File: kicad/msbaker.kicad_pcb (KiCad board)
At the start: 4 copper layers, 14 x 62 mm, 41 parts, among them J1 USB_B_Micro, J2 Micro_SD_Card, J3 GPIO, M2 MountingHole_2.2mm_M2_ISO1458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, U1 MIC5365-3.3YC5, U2 W25Q128JVS, U3 RP2040, U4 LSM6DSO32, Y1 12MHz

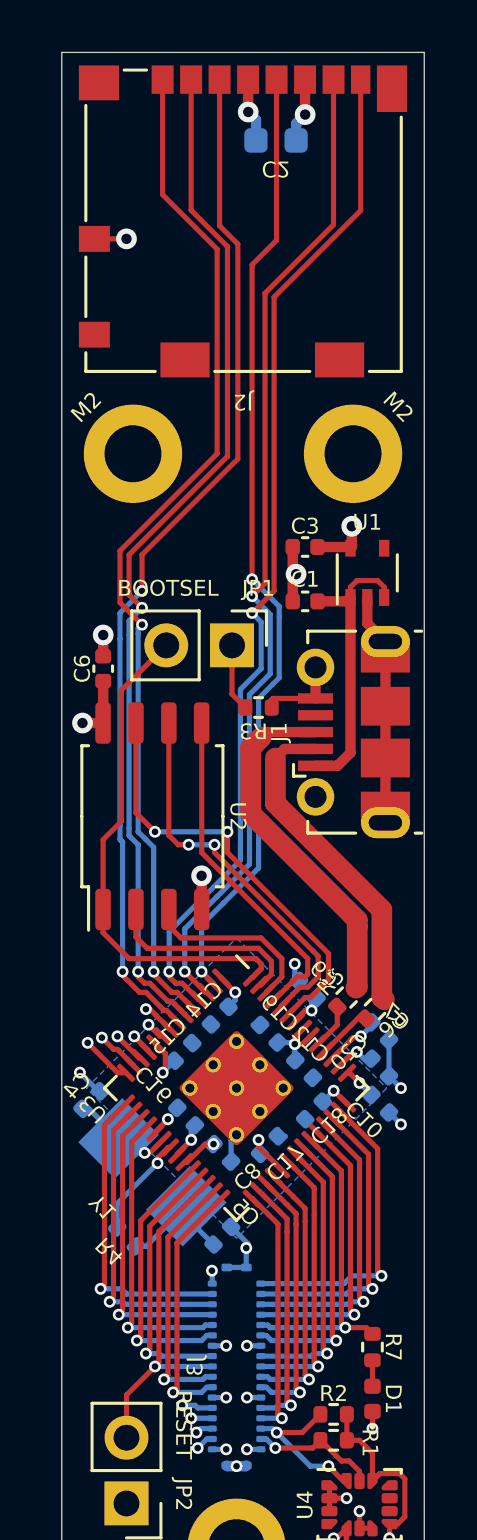
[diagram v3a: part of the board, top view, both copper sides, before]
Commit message: Fixed DRC violations
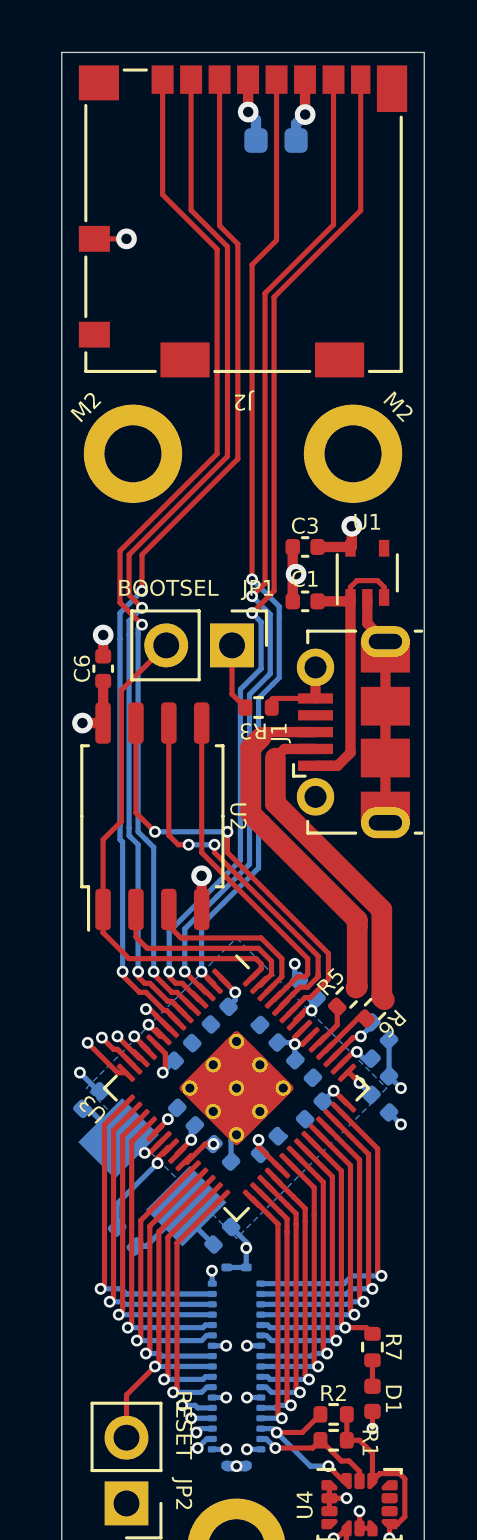
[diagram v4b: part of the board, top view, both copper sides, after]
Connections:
- J3 pad GND: (no net) -> GND
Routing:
- net GND: track 37.7 -> 38.5 mm, vias 21 -> 22
- net (no net): track 0.77 -> 0.00 mm, vias 1 -> 0
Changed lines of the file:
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@@
     (property "Sheetname" "")
     (attr smd)
-    (fp_text reference "C9" (at 0 0.848528 315 unlocked) (layer "F.SilkS")
+    (fp_text reference "C9" (at 0 0.848528 315 unlocked) (layer "B.SilkS")
       (effects (font (size 0.61 0.61) (thickness 0.0762)) (justify mirror))
     )
@@
     (property "Sheetname" "")
     (attr smd)
-    (fp_text reference "C19" (at 0.282843 0.848528 315 unlocked) (layer "F.SilkS")
+    (fp_text reference "C19" (at 0.282843 0.848528 315 unlocked) (layer "B.SilkS")
       (effects (font (size 0.61 0.61) (thickness 0.0762)) (justify mirror))
     )
@@
     (property "Sheetname" "")
     (attr smd)
-    (fp_text reference "C10" (at 0 0.848528 135 unlocked) (layer "F.SilkS")
+    (fp_text reference "C10" (at 0 0.848528 135 unlocked) (layer "B.SilkS")
       (effects (font (size 0.61 0.61) (thickness 0.0762)) (justify mirror))
     )
@@
     (property "Sheetname" "")
     (attr smd)
-    (fp_text reference "C12" (at -0.50995 -0.848528 -45 unlocked) (layer "F.SilkS")
+    (fp_text reference "C12" (at -0.50995 -0.848528 -45 unlocked) (layer "B.SilkS")
       (effects (font (size 0.61 0.61) (thickness 0.0762)) (justify mirror))
     )
@@
     (property "Sheetname" "")
     (attr smd)
-    (fp_text reference "C18" (at 0.02038 -0.813173 -135 unlocked) (layer "F.SilkS")
+    (fp_text reference "C18" (at 0.02038 -0.813173 -135 unlocked) (layer "B.SilkS")
       (effects (font (size 0.61 0.61) (thickness 0.0762)) (justify mirror))
     )
@@
     (property "Sheetname" "")
     (attr smd)
-    (fp_text reference "C15" (at 0 -0.848528 45 unlocked) (layer "F.SilkS")
+    (fp_text reference "C15" (at 0 -0.848528 45 unlocked) (layer "B.SilkS")
       (effects (font (size 0.61 0.61) (thickness 0.0762)) (justify mirror))
     )
@@
     (property "Sheetname" "")
     (attr smd)
-    (fp_text reference "C16" (at 1.767767 0 135 unlocked) (layer "F.SilkS")
+    (fp_text reference "C16" (at 1.767767 0 135 unlocked) (layer "B.SilkS")
       (effects (font (size 0.61 0.61) (thickness 0.0762)) (justify mirror))
     )
@@
     (property "Sheetname" "")
     (attr smd)
-    (fp_text reference "C17" (at -0.035355 0.883883 225 unlocked) (layer "F.SilkS")
+    (fp_text reference "C17" (at -0.035355 0.883883 225 unlocked) (layer "B.SilkS")
       (effects (font (size 0.61 0.61) (thickness 0.0762)) (justify mirror))
     )
@@
     (property "Sheetname" "")
     (attr smd)
-    (fp_text reference "J3" (at 0 1.6 90 unlocked) (layer "F.SilkS")
+    (fp_text reference "J3" (at 0 1.6 90 unlocked) (layer "B.SilkS")
       (effects (font (size 0.61 0.61) (thickness 0.0762)) (justify mirror))
     )
@@
     (pad "34" smd roundrect (at 3.2 0.9375 270) (size 0.24 0.35) (layers "B.Cu" "B.Paste" "B.Mask") (roundrect_rratio 0.25)
       (net 2 "GND") (pinfunction "Pin_34") (pintype "passive"))
-    (pad "GND" smd roundrect (at 3.825 0.375 270) (size 0.3 0.42) (layers "B.Cu" "B.Paste" "B.Mask") (roundrect_rratio 0.25))
-    (pad "GND" smd roundrect (at -3.825 0.375 270) (size 0.3 0.42) (layers "B.Cu" "B.Paste" "B.Mask") (roundrect_rratio 0.25))
-    (pad "GND" smd roundrect (at -3.825 -0.375 270) (size 0.3 0.42) (layers "B.Cu" "B.Paste" "B.Mask") (roundrect_rratio 0.25))
-    (pad "GND" smd roundrect (at 3.825 -0.375 270) (size 0.3 0.42) (layers "B.Cu" "B.Paste" "B.Mask") (roundrect_rratio 0.25))
+    (pad "GND" smd roundrect (at 3.825 0.375 270) (size 0.3 0.42) (layers "B.Cu" "B.Paste" "B.Mask") (roundrect_rratio 0.25)
+      (net 2 "GND"))
+    (pad "GND" smd roundrect (at -3.825 0.375 270) (size 0.3 0.42) (layers "B.Cu" "B.Paste" "B.Mask") (roundrect_rratio 0.25)
+      (net 2 "GND"))
+    (pad "GND" smd roundrect (at -3.825 -0.375 270) (size 0.3 0.42) (layers "B.Cu" "B.Paste" "B.Mask") (roundrect_rratio 0.25)
+      (net 2 "GND"))
+    (pad "GND" smd roundrect (at 3.825 -0.375 270) (size 0.3 0.42) (layers "B.Cu" "B.Paste" "B.Mask") (roundrect_rratio 0.25)
+      (net 2 "GND"))
   )
   (footprint "Capacitor_SMD:C_0603_1608Metric" (layer "B.Cu")
@@
     (property "Sheetname" "")
     (attr smd)
-    (fp_text reference "C2" (at 0 1.1 180 unlocked) (layer "F.SilkS")
+    (fp_text reference "C2" (at 0 1.1 180 unlocked) (layer "B.SilkS")
       (effects (font (size 0.61 0.61) (thickness 0.0762)) (justify mirror))
     )
@@
     (property "Sheetname" "")
     (attr smd)
-    (fp_text reference "Y1" (at 0.388909 -2.298097 135 unlocked) (layer "F.SilkS")
+    (fp_text reference "Y1" (at 0.388909 -2.298097 135 unlocked) (layer "B.SilkS")
       (effects (font (size 0.61 0.61) (thickness 0.0762)) (justify mirror))
     )
@@
     (property "Sheetname" "")
     (attr smd)
-    (fp_text reference "C14" (at 0 0.848528 45 unlocked) (layer "F.SilkS")
+    (fp_text reference "C14" (at 0 0.848528 45 unlocked) (layer "B.SilkS")
       (effects (font (size 0.61 0.61) (thickness 0.0762)) (justify mirror))
     )
@@
     (property "Sheetname" "")
     (attr smd)
-    (fp_text reference "C4" (at -0.014975 0.777817 45 unlocked) (layer "F.SilkS")
+    (fp_text reference "C4" (at -0.014975 0.777817 45 unlocked) (layer "B.SilkS")
       (effects (font (size 0.61 0.61) (thickness 0.0762)) (justify mirror))
     )
@@
     (property "Sheetname" "")
     (attr smd)
-    (fp_text reference "C7" (at 0.035355 -0.813173 -45 unlocked) (layer "F.SilkS")
+    (fp_text reference "C7" (at 0.035355 -0.813173 -45 unlocked) (layer "B.SilkS")
       (effects (font (size 0.61 0.61) (thickness 0.0762)) (justify mirror))
     )
@@
     (property "Sheetname" "")
     (attr smd)
-    (fp_text reference "R4" (at 0.070711 -0.848528 135 unlocked) (layer "F.SilkS")
+    (fp_text reference "R4" (at 0.070711 -0.848528 135 unlocked) (layer "B.SilkS")
       (effects (font (size 0.61 0.61) (thickness 0.0762)) (justify mirror))
     )
@@
     (property "Sheetname" "")
     (attr smd)
-    (fp_text reference "C5" (at -1.272792 0 -45 unlocked) (layer "F.SilkS")
+    (fp_text reference "C5" (at -1.272792 0 -45 unlocked) (layer "B.SilkS")
       (effects (font (size 0.61 0.61) (thickness 0.0762)) (justify mirror))
     )
@@
     (property "Sheetname" "")
     (attr smd)
-    (fp_text reference "C20" (at -1.272792 0.424264 45 unlocked) (layer "F.SilkS")
+    (fp_text reference "C20" (at -1.272792 0.424264 45 unlocked) (layer "B.SilkS")
       (effects (font (size 0.61 0.61) (thickness 0.0762)) (justify mirror))
     )
@@
     (property "Sheetname" "")
     (attr smd)
-    (fp_text reference "C8" (at 1.308148 -0.035355 225 unlocked) (layer "F.SilkS")
+    (fp_text reference "C8" (at 1.308148 -0.035355 225 unlocked) (layer "B.SilkS")
       (effects (font (size 0.61 0.61) (thickness 0.0762)) (justify mirror))
     )
@@
   )
   (gr_rect (start 177.5 67.5) (end 191.5 129.5) (layer "Edge.Cuts") (width 0.05) (fill none))
-  (via (at 184.25 122.1) (size 0.457) (drill 0.254) (layers "F.Cu" "B.Cu") (net 0))
-  (segment (start 184.25 122.1) (end 184.6 122.1) (width 0.4) (layer "B.Cu") (net 0))
-  (segment (start 183.875 122.075) (end 183.9 122.1) (width 0.4) (layer "B.Cu") (net 0))
-  (segment (start 183.9 122.1) (end 184.25 122.1) (width 0.4) (layer "B.Cu") (net 0))
-  (segment (start 184.6 122.1) (end 184.625 122.075) (width 0.4) (layer "B.Cu") (net 0))
   (segment (start 188.65 88.55) (end 188.65 88.15) (width 0.2) (layer "F.Cu") (net 1))
   (segment (start 189.7 87.9) (end 189.95 88.15) (width 0.2) (layer "F.Cu") (net 1))
@@
   (via (at 178.2 106.9) (size 0.457) (drill 0.254) (layers "F.Cu" "B.Cu") (net 2))
   (via (at 190.6 108.9) (size 0.457) (drill 0.254) (layers "F.Cu" "B.Cu") (net 2))
+  (via (at 184.25 122.1) (size 0.457) (drill 0.254) (layers "F.Cu" "B.Cu") (net 2))
   (segment (start 186.660589 103.360589) (end 186.5 103.2) (width 0.2) (layer "B.Cu") (net 2))
   (segment (start 184.25 109.45) (end 184.25 109.303122) (width 0.2) (layer "B.Cu") (net 2))
@@
   (segment (start 184.625 113.675) (end 184.7 113.6) (width 0.2) (layer "B.Cu") (net 2))
   (segment (start 181.6 108.621178) (end 181.6 108.7) (width 0.2) (layer "B.Cu") (net 2))
+  (segment (start 184.25 122.1) (end 184.6 122.1) (width 0.4) (layer "B.Cu") (net 2))
   (segment (start 186.55 70.9) (end 186.55 70.25) (width 0.4) (layer "B.Cu") (net 2))
+  (segment (start 183.875 122.075) (end 183.9 122.1) (width 0.4) (layer "B.Cu") (net 2))
   (segment (start 190.139411 105.639411) (end 190.139411 107.039411) (width 0.2) (layer "B.Cu") (net 2))
   (segment (start 178.978822 107.621178) (end 178.921178 107.621178) (width 0.2) (layer "B.Cu") (net 2))
@@
   (segment (start 178.921178 107.621178) (end 178.2 106.9) (width 0.2) (layer "B.Cu") (net 2))
   (segment (start 183.875 114.425) (end 184.625 114.425) (width 0.2) (layer "B.Cu") (net 2))
+  (segment (start 183.9 122.1) (end 184.25 122.1) (width 0.4) (layer "B.Cu") (net 2))
   (segment (start 185.839411 109.360589) (end 186.139411 109.360589) (width 0.2) (layer "B.Cu") (net 2))
   (segment (start 183.3125 117.45) (end 183.85 117.45) (width 0.2) (layer "B.Cu") (net 2))
@@
   (segment (start 183.348439 106.569617) (end 183.348439 106.598439) (width 0.2) (layer "B.Cu") (net 2))
   (segment (start 185.1875 121.45) (end 184.65 121.45) (width 0.2) (layer "B.Cu") (net 2))
+  (segment (start 184.6 122.1) (end 184.625 122.075) (width 0.4) (layer "B.Cu") (net 2))
   (segment (start 190.139411 108.439411) (end 190.6 108.9) (width 0.2) (layer "B.Cu") (net 2))
   (segment (start 185.839411 109.360589) (end 185.839411 109.089411) (width 0.2) (layer "B.Cu") (net 2))
